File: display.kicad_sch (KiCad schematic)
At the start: 17 parts, among them Q5 Q_NMOS_DGS, U12 E2266CS0C2

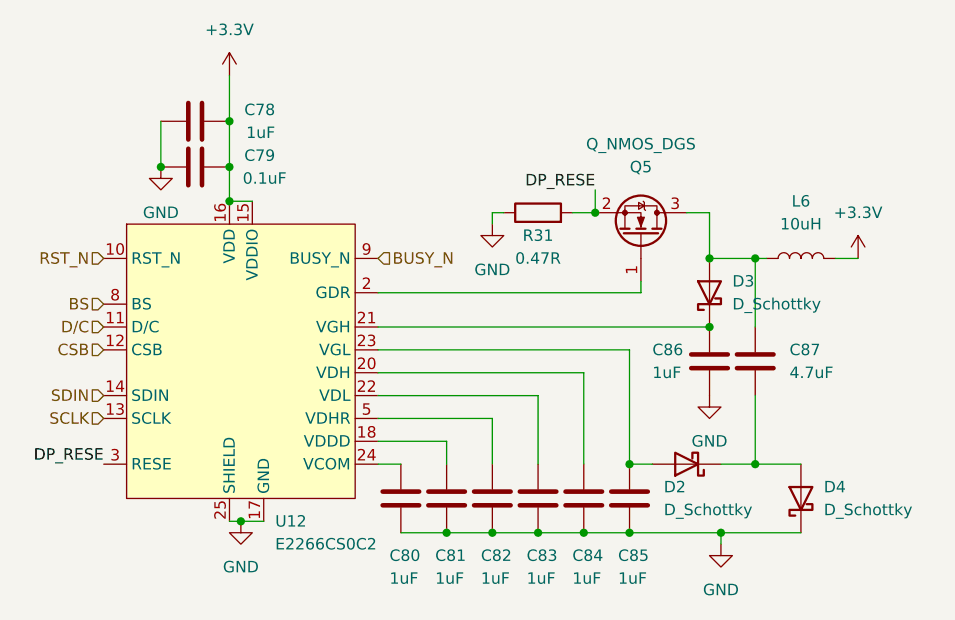
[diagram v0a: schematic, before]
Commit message: done first iteration of pcb routing, slikscreen still broken
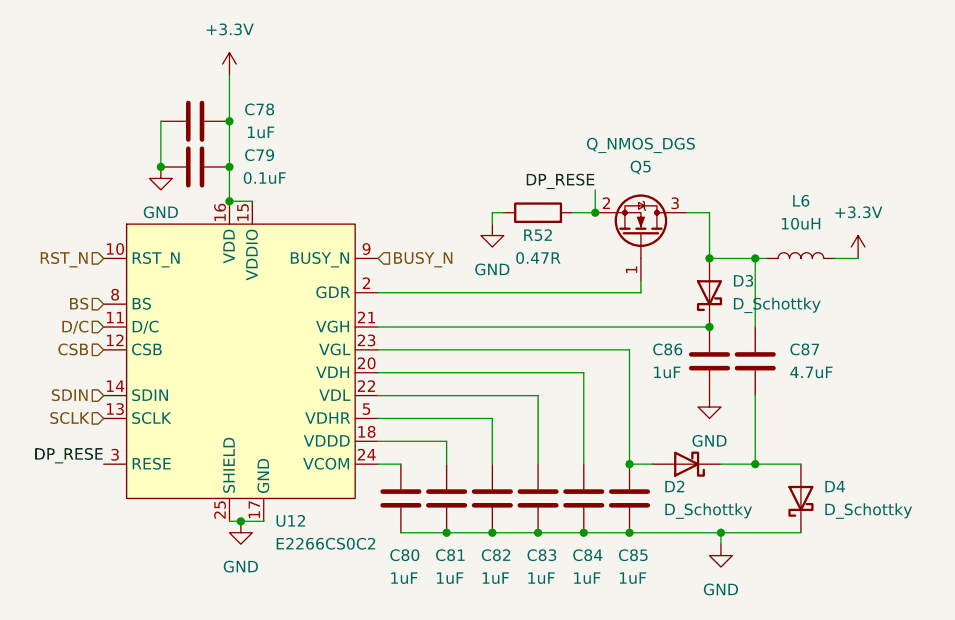
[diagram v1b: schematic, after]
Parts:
- renumbered R31 to R52
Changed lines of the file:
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@@
   (symbol (lib_id "power:GND") (at 196.85 96.52 0) (unit 1)
     (in_bom yes) (on_board yes) (fields_autoplaced)
-    (property "Reference" "#PWR099" (id 0) (at 196.85 102.87 0)
+    (property "Reference" "#PWR0102" (id 0) (at 196.85 102.87 0)
       (effects (font (size 1.27 1.27)) hide)
     )
@@
   (symbol (lib_id "power:GND") (at 135.89 71.12 0) (unit 1)
     (in_bom yes) (on_board yes) (fields_autoplaced)
-    (property "Reference" "#PWR095" (id 0) (at 135.89 77.47 0)
+    (property "Reference" "#PWR098" (id 0) (at 135.89 77.47 0)
       (effects (font (size 1.27 1.27)) hide)
     )
@@
   (symbol (lib_id "power:GND") (at 144.78 110.49 0) (unit 1)
     (in_bom yes) (on_board yes) (fields_autoplaced)
-    (property "Reference" "#PWR097" (id 0) (at 144.78 116.84 0)
+    (property "Reference" "#PWR0100" (id 0) (at 144.78 116.84 0)
       (effects (font (size 1.27 1.27)) hide)
     )
@@
   (symbol (lib_id "power:+3.3V") (at 143.51 60.96 0) (unit 1)
     (in_bom yes) (on_board yes) (fields_autoplaced)
-    (property "Reference" "#PWR096" (id 0) (at 143.51 64.77 0)
+    (property "Reference" "#PWR099" (id 0) (at 143.51 64.77 0)
       (effects (font (size 1.27 1.27)) hide)
     )
@@
   (symbol (lib_id "power:+3.3V") (at 213.36 81.28 0) (unit 1)
     (in_bom yes) (on_board yes) (fields_autoplaced)
-    (property "Reference" "#PWR0101" (id 0) (at 213.36 85.09 0)
+    (property "Reference" "#PWR0104" (id 0) (at 213.36 85.09 0)
       (effects (font (size 1.27 1.27)) hide)
     )
@@
   (symbol (lib_id "power:GND") (at 172.72 77.47 0) (unit 1)
     (in_bom yes) (on_board yes) (fields_autoplaced)
-    (property "Reference" "#PWR098" (id 0) (at 172.72 83.82 0)
+    (property "Reference" "#PWR0101" (id 0) (at 172.72 83.82 0)
       (effects (font (size 1.27 1.27)) hide)
     )
@@
   (symbol (lib_id "Device:R") (at 177.8 76.2 90) (unit 1)
     (in_bom yes) (on_board yes)
-    (property "Reference" "R31" (id 0) (at 177.8 78.74 90))
+    (property "Reference" "R52" (id 0) (at 177.8 78.74 90))
     (property "Value" "0.47R" (id 1) (at 177.8 81.28 90))
     (property "Footprint" "Resistor_SMD:R_0603_1608Metric_Pad0.98x0.95mm_HandSolder" (id 2) (at 177.8 77.978 90)
@@
   (symbol (lib_id "power:GND") (at 198.12 113.03 0) (unit 1)
     (in_bom yes) (on_board yes) (fields_autoplaced)
-    (property "Reference" "#PWR0100" (id 0) (at 198.12 119.38 0)
-      (effects (font (size 1.27 1.27)) hide)
-    )
+    (property "Reference" "#PWR0103" (id 0) (at 198.12 119.38 0)
+      (effects (font (size 1.27 1.27)) hide)
+    )

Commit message: mounting holes, fixes silkscreen
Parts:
- renumbered R52 to R51
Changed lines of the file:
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@@
   (symbol (lib_id "Device:R") (at 177.8 76.2 90) (unit 1)
     (in_bom yes) (on_board yes)
-    (property "Reference" "R52" (id 0) (at 177.8 78.74 90))
+    (property "Reference" "R51" (id 0) (at 177.8 78.74 90))
     (property "Value" "0.47R" (id 1) (at 177.8 81.28 90))
     (property "Footprint" "Resistor_SMD:R_0603_1608Metric_Pad0.98x0.95mm_HandSolder" (id 2) (at 177.8 77.978 90)
